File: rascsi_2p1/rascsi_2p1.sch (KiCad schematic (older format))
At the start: 92 parts, among them IC1 SN74LS245DW, IC2 SN74LS245DW, IC3 SN74LS245DW, IC4 SN74LS245DW, J1 Raspberry_Pi_2_3, J2 Conn_01x02_Male, J3 Conn_02x25_Odd_Even, J4 I2C Pinout, J5 L717SDB25PA4CH4F, X1 Mac, X2 Dogcow, X3 Mac2, X4 Raspberry Pi, X5 Dogcow2, X6 Mac Trashcan, X7 Pi, X8 Pi

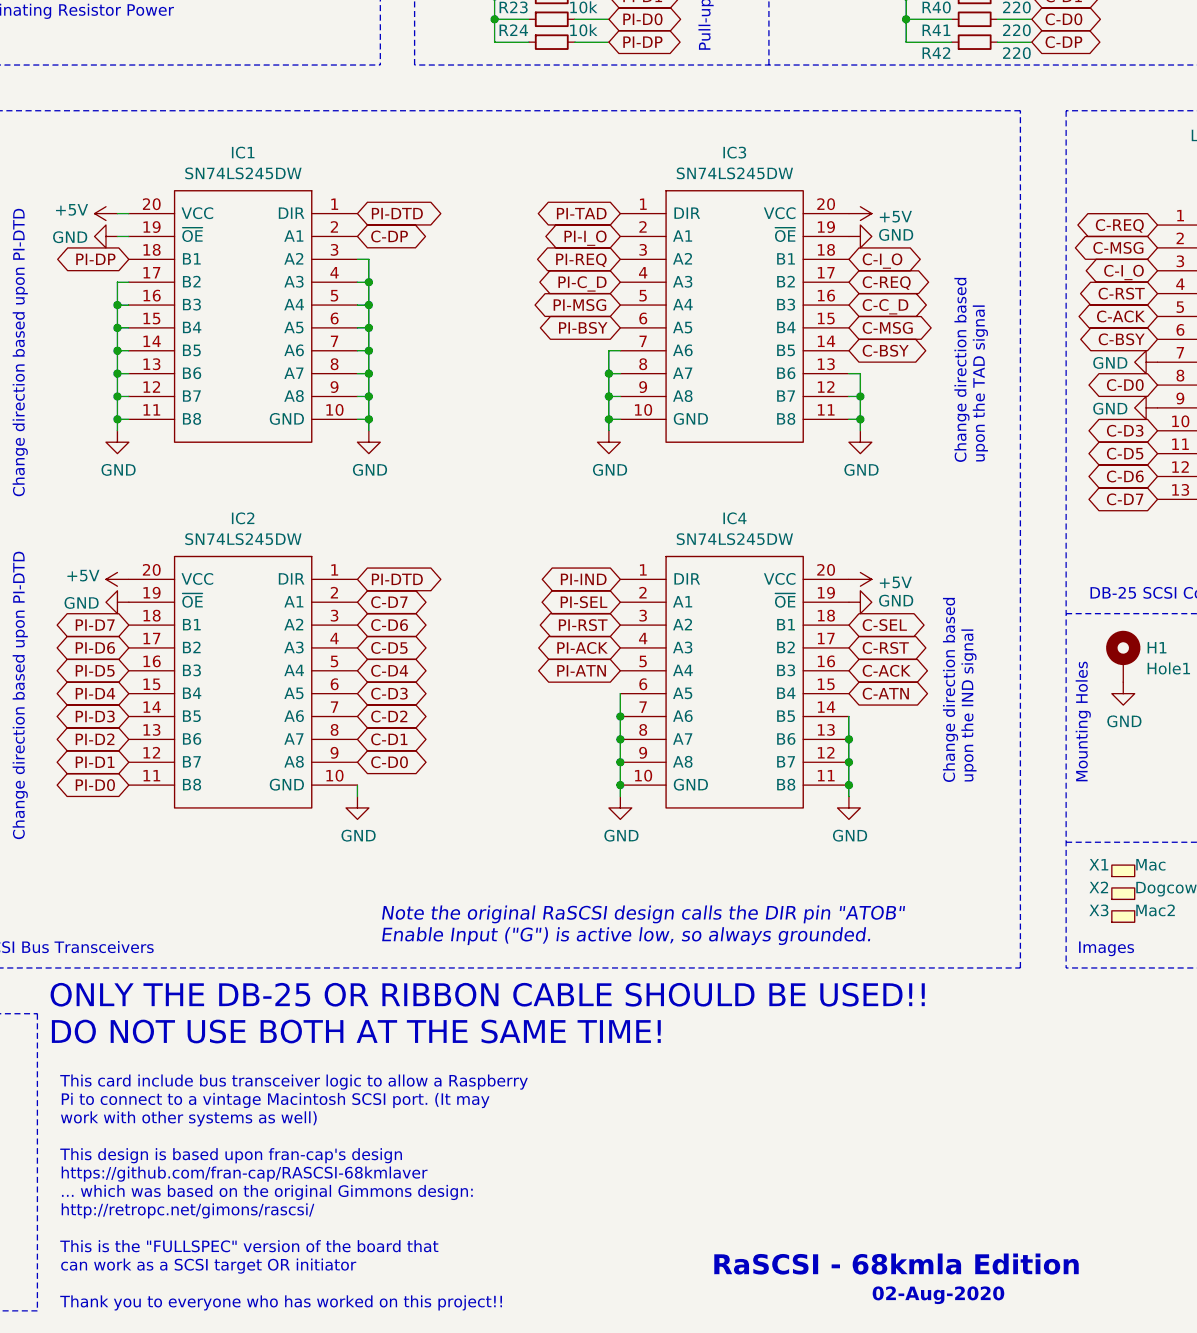
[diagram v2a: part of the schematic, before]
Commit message: Changed Bus Transceivers to 74LS641-1 per discussion on 68kmla forums
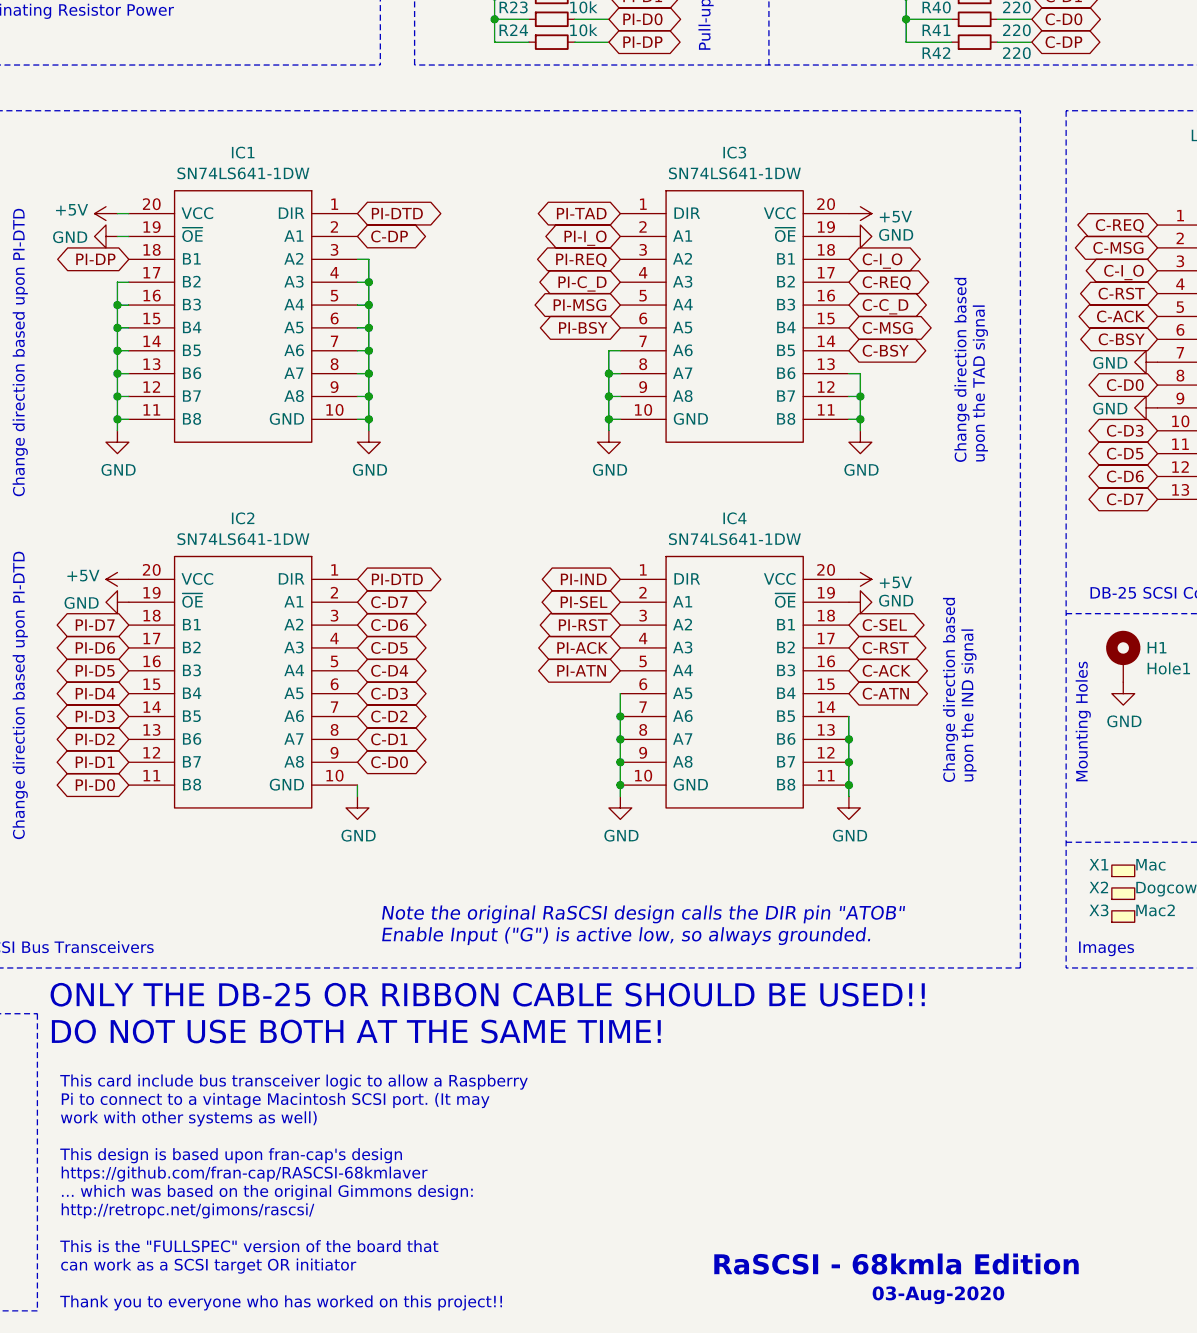
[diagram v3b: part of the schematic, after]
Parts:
- IC1, IC2, IC3, IC4: value SN74LS245DW -> SN74LS641-1DW; LCSC C129580 -> (none); Manufacturer_Part_Number SN74LS245DW -> SN74LS641-1DW; Mouser Part Number 595-SN74LS245DW -> (none); Mouser Price/Stock https://www.mouser.co.uk/ProductDetail/Texas-Instruments/SN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 -> (none)
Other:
- note added: "03-Aug-2020"
- note removed: "02-Aug-2020"
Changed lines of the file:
@@
 P 5200 3100
 F 0 "IC1" H 5700 3365 50  0000 C CNN
-F 1 "SN74LS245DW" H 5700 3274 50  0000 C CNN
+F 1 "SN74LS641-1DW" H 5700 3274 50  0000 C CNN
 F 2 "SOIC127P1030X265-20N" H 6050 3200 50  0001 L CNN
-F 3 "http://www.ti.com/lit/gpn/sn74ls245" H 6050 3100 50  0001 L CNN
+F 3 "https://www.ti.com/lit/ds/symlink/sn74ls641.pdf?ts=1596466276486&ref_url=https%253A%252F%252Fwww.ti.com%252Fstore%252Fti%252Fen%252Fp%252Fproduct%252F%253Fp%253DSN74LS641-1DW" H 6050 3100 50  0001 L CNN
 F 4 "Octal bus transceivers" H 6050 3000 50  0001 L CNN "Description"
 F 5 "2.65" H 6050 2900 50  0001 L CNN "Height"
-F 6 "595-SN74LS245DW" H 6050 2800 50  0001 L CNN "Mouser Part Number"
-F 7 "https://www.mouser.co.uk/ProductDetail/Texas-Instruments/SN74LS245DW?qs=ZA235jQDfbpxKQZqDHbgmw%3D%3D" H 6050 2700 50  0001 L CNN "Mouser Price/Stock"
+F 6 "" H 6050 2800 50  0001 L CNN "Mouser Part Number"
+F 7 "" H 6050 2700 50  0001 L CNN "Mouser Price/Stock"
 F 8 "Texas Instruments" H 6050 2600 50  0001 L CNN "Manufacturer_Name"
-F 9 "SN74LS245DW" H 6050 2500 50  0001 L CNN "Manufacturer_Part_Number"
-F 10 "C129580" H 5200 3100 50  0001 C CNN "LCSC"
+F 9 "SN74LS641-1DW" H 6050 2500 50  0001 L CNN "Manufacturer_Part_Number"
+F 10 "" H 5200 3100 50  0001 C CNN "LCSC"
 	1    5200 3100
 	-1   0    0    -1
@@
 P 5200 4700
 F 0 "IC2" H 5700 4965 50  0000 C CNN
-F 1 "SN74LS245DW" H 5700 4874 50  0000 C CNN
+F 1 "SN74LS641-1DW" H 5700 4874 50  0000 C CNN
 F 2 "SOIC127P1030X265-20N" H 6050 4800 50  0001 L CNN
-F 3 "http://www.ti.com/lit/gpn/sn74ls245" H 6050 4700 50  0001 L CNN
+F 3 "https://www.ti.com/lit/ds/symlink/sn74ls641.pdf?ts=1596466276486&ref_url=https%253A%252F%252Fwww.ti.com%252Fstore%252Fti%252Fen%252Fp%252Fproduct%252F%253Fp%253DSN74LS641-1DW" H 6050 4700 50  0001 L CNN
 F 4 "Octal bus transceivers" H 6050 4600 50  0001 L CNN "Description"
 F 5 "2.65" H 6050 4500 50  0001 L CNN "Height"
-F 6 "595-SN74LS245DW" H 6050 4400 50  0001 L CNN "Mouser Part Number"
-F 7 "https://www.mouser.co.uk/ProductDetail/Texas-Instruments/SN74LS245DW?qs=ZA235jQDfbpxKQZqDHbgmw%3D%3D" H 6050 4300 50  0001 L CNN "Mouser Price/Stock"
+F 6 "" H 6050 4400 50  0001 L CNN "Mouser Part Number"
+F 7 "" H 6050 4300 50  0001 L CNN "Mouser Price/Stock"
 F 8 "Texas Instruments" H 6050 4200 50  0001 L CNN "Manufacturer_Name"
-F 9 "SN74LS245DW" H 6050 4100 50  0001 L CNN "Manufacturer_Part_Number"
-F 10 "C129580" H 5200 4700 50  0001 C CNN "LCSC"
+F 9 "SN74LS641-1DW" H 6050 4100 50  0001 L CNN "Manufacturer_Part_Number"
+F 10 "" H 5200 4700 50  0001 C CNN "LCSC"
 	1    5200 4700
 	-1   0    0    -1
@@
 P 6350 3100
 F 0 "IC3" H 6850 3365 50  0000 C CNN
-F 1 "SN74LS245DW" H 6850 3274 50  0000 C CNN
+F 1 "SN74LS641-1DW" H 6850 3274 50  0000 C CNN
 F 2 "SOIC127P1030X265-20N" H 7200 3200 50  0001 L CNN
-F 3 "http://www.ti.com/lit/gpn/sn74ls245" H 7200 3100 50  0001 L CNN
+F 3 "https://www.ti.com/lit/ds/symlink/sn74ls641.pdf?ts=1596466276486&ref_url=https%253A%252F%252Fwww.ti.com%252Fstore%252Fti%252Fen%252Fp%252Fproduct%252F%253Fp%253DSN74LS641-1DW" H 7200 3100 50  0001 L CNN
 F 4 "Octal bus transceivers" H 7200 3000 50  0001 L CNN "Description"
 F 5 "2.65" H 7200 2900 50  0001 L CNN "Height"
-F 6 "595-SN74LS245DW" H 7200 2800 50  0001 L CNN "Mouser Part Number"
-F 7 "https://www.mouser.co.uk/ProductDetail/Texas-Instruments/SN74LS245DW?qs=ZA235jQDfbpxKQZqDHbgmw%3D%3D" H 7200 2700 50  0001 L CNN "Mouser Price/Stock"
+F 6 "" H 7200 2800 50  0001 L CNN "Mouser Part Number"
+F 7 "" H 7200 2700 50  0001 L CNN "Mouser Price/Stock"
 F 8 "Texas Instruments" H 7200 2600 50  0001 L CNN "Manufacturer_Name"
-F 9 "SN74LS245DW" H 7200 2500 50  0001 L CNN "Manufacturer_Part_Number"
-F 10 "C129580" H 6350 3100 50  0001 C CNN "LCSC"
+F 9 "SN74LS641-1DW" H 7200 2500 50  0001 L CNN "Manufacturer_Part_Number"
+F 10 "" H 6350 3100 50  0001 C CNN "LCSC"
 	1    6350 3100
 	1    0    0    -1
@@
 P 6350 4700
 F 0 "IC4" H 6850 4965 50  0000 C CNN
-F 1 "SN74LS245DW" H 6850 4874 50  0000 C CNN
+F 1 "SN74LS641-1DW" H 6850 4874 50  0000 C CNN
 F 2 "SOIC127P1030X265-20N" H 7200 4800 50  0001 L CNN
-F 3 "http://www.ti.com/lit/gpn/sn74ls245" H 7200 4700 50  0001 L CNN
+F 3 "https://www.ti.com/lit/ds/symlink/sn74ls641.pdf?ts=1596466276486&ref_url=https%253A%252F%252Fwww.ti.com%252Fstore%252Fti%252Fen%252Fp%252Fproduct%252F%253Fp%253DSN74LS641-1DW" H 7200 4700 50  0001 L CNN
 F 4 "Octal bus transceivers" H 7200 4600 50  0001 L CNN "Description"
 F 5 "2.65" H 7200 4500 50  0001 L CNN "Height"
-F 6 "595-SN74LS245DW" H 7200 4400 50  0001 L CNN "Mouser Part Number"
-F 7 "https://www.mouser.co.uk/ProductDetail/Texas-Instruments/SN74LS245DW?qs=ZA235jQDfbpxKQZqDHbgmw%3D%3D" H 7200 4300 50  0001 L CNN "Mouser Price/Stock"
+F 6 "" H 7200 4400 50  0001 L CNN "Mouser Part Number"
+F 7 "" H 7200 4300 50  0001 L CNN "Mouser Price/Stock"
 F 8 "Texas Instruments" H 7200 4200 50  0001 L CNN "Manufacturer_Name"
-F 9 "SN74LS245DW" H 7200 4100 50  0001 L CNN "Manufacturer_Part_Number"
-F 10 "C129580" H 6350 4700 50  0001 C CNN "LCSC"
+F 9 "SN74LS641-1DW" H 7200 4100 50  0001 L CNN "Manufacturer_Part_Number"
+F 10 "" H 6350 4700 50  0001 C CNN "LCSC"
 	1    6350 4700
 	1    0    0    -1
@@
 2.1a
 Text Notes 7450 7870 0    59   ~ 12
-02-Aug-2020
+03-Aug-2020
 Wire Wire Line
 	2850 6050 2950 6050
